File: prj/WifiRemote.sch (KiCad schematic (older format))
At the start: 52 parts, among them J1 DIP-BLACK-MALE-HEADER-VERT_4P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, J2 DIP-BLACK-MALE-HEADER_6P-2.54_, K1 DIP-SWITCH-TACTILE-SPST-NO_TS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, K2 DIP-SWITCH-TACTILE-SPST-NO_TS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, K3 DIP-SWITCH-TACTILE-SPST-NO_TS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, K4 DIP-SWITCH-TACTILE-SPST-NO_TS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, SW1 DIP-TOGGLE-SWITCH-ON-ON_3+2P-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, U1 CONTROLLER-ESP8266, U2 BOOST-MCP1642B-ADJI/MC-MSOP8

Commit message: Updated ADC input for 3V input (2x AA's)
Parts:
- removed R2: SMD-RES-10K-1%-1_10W_0603_, SeeedOPL-Resistor-2016:R0603, symbol SMD-RES-10K-1%-1_10W_0603_
- added R1: SMD-RES-2.7K-1%-1_16W_0402_, symbol SMD-RES-2.7K-1%-1_16W_0402_
- renumbered C2 to C1, C3 to C2, C4 to C3, C5 to C4, C1 to C5, D3 to D1, D4 to D2, D1 to D3, D2 to D4, R12 to R11, R13 to R12, R14 to R13, R16 to R14, R1 to R15, R4 to R16, R11 to R17, R15 to R18, R17 to R19, R3 to R2, R18 to R20, R19 to R21, R20 to R22, R21 to R23, R22 to R24, R23 to R25, R6 to R3, R7 to R4, R24 to R6, R25 to R7

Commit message: Added battery monitoring LED, changed ADC resistor divider, and added ESD + reverse polarity protection on battery
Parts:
- removed R1: SMD-RES-2.7K-1%-1_16W_0402_, symbol SMD-RES-2.7K-1%-1_16W_0402_
- removed R9: SMD-RES-1K-1%-1_10W_0603_, SeeedOPL-Resistor-2016:R0603, symbol SMD-RES-1K-1%-1_10W_0603_
- added D?: SMD-LED-CLEAR-RED_0805_, symbol SMD-LED-CLEAR-RED_0805_
- added D?: SMD-Diode-TVS-3.3VMW-15V-SOD-523, Diodes_SMD:SOD-523, symbol SMD-Diode-TVS-3.3VMW-15V-SOD-523
- added Q?: SMD-MOSFET-N-CH-20V-2.1A-CJ2302_SOT-23_, symbol SMD-MOSFET-N-CH-20V-2.1A-CJ2302_SOT-23_
- added R?: SMD-RES-20K-1%-1_10W_0603_, symbol SMD-RES-20K-1%-1_10W_0603_
- added R?: SMD-RES-51K-5%-1_10W_0603_, symbol SMD-RES-51K-5%-1_10W_0603_
- added R?: SMD-RES-10R-5%-1_10W_0603_, SeeedOPL-Resistor-2016:R0603, symbol SMD-RES-10R-5%-1_10W_0603_
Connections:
- wire segments 100 -> 105
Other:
- note added: "Is BATT- a different GND potential?"
- moved on the sheet: C1, C2, C3, D1, D2, L1, R10, R11, R12, R13, R5, R6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

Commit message: Added button debounce, rev polarity prot, updated ESP-12F, added red LED, updated ADC resistor values
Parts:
- removed D6, D8: SMD-Diode-TVS-3.3VMW-15V-SOD-523, Diodes_SMD:SOD-523, symbol SMD-Diode-TVS-3.3VMW-15V-SOD-523
- removed Q?: SMD-MOSFET-N-CH-20V-2.1A-CJ2302_SOT-23_, symbol SMD-MOSFET-N-CH-20V-2.1A-CJ2302_SOT-23_
- added C6, C7, C8, C9: CERAMIC-100NF-50V-10%-X7R_0603_, symbol CERAMIC-100NF-50V-10%-X7R_0603_
- added D12, D13: SMD-Diode-TVS-3.3VMW-15V-SOD-523, Diodes_SMD:SOD-523, symbol SMD-Diode-TVS-3.3VMW-15V-SOD-523
- added Q1: SMD-MOSFET-P-CH-20V-2A-FDN340P_SOT-23_, symbol SMD-MOSFET-P-CH-20V-2A-FDN340P_SOT-23_
- added R27, R28, R29, R30: SMD-RES-200R-5%-1_10W_0603_, symbol SMD-RES-200R-5%-1_10W_0603_
- R6, R7: RESISTANCE 10 -> 10R
- R8: renamed from R?; RESISTANCE 10 -> 10R
- U1: PART NUMBER ESP-12E -> ESP-12F; SKU 310060021 -> 317060163; SUPPLIER ITEAD -> (none); SUPPLIER PART ESP-12E -> (none)
- gave numbers to parts that had none: 4
- renumbered D12 to D14, D3 to D5, D4 to D6, D5 to D7, D7 to D8, R10 to R11, R11 to R12, R12 to R13, R13 to R14, R14 to R15, R15 to R16, R16 to R17, R17 to R18, R18 to R19, R19 to R20, R20 to R21, R21 to R22, R22 to R23, R23 to R24, R24 to R25, R25 to R26, R8 to R9
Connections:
- wire segments 105 -> 128
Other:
- note removed: "Is BATT- a different GND potential?"
- moved on the sheet: D11, D14, D7, D8, D9, K1, K2, K3, K4, R21, R22, R23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

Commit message: Updated footprints and removed ESP-12F incorrect footprint
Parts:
- C6, C7, C8, C9: footprint (none) -> SeeedOPL-Capacitor-2016:C0603
- D3: footprint (none) -> SeeedOPL-LED-2016:LED-0805
- Q1: footprint (none) -> SeeedOPL-Transistor-2016:SOT-23
- R1, R10, R27, R28, R29, R30: footprint (none) -> SeeedOPL-Resistor-2016:R0603
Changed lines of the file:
@@
 F 0 "R10" V 6550 1650 45  0000 L BNN
 F 1 "SMD-RES-20K-1%-1_10W_0603_" H 6400 1500 45  0001 L BNN
-F 2 "" H 6550 1600 40  0001 C CNN
+F 2 "SeeedOPL-Resistor-2016:R0603" H 6550 1600 40  0001 C CNN
 F 3 "" H 6550 1600 40  0001 C CNN
 F 4 "RC0603FR-0720KL" H 6580 1750 20  0001 C CNN "MPN"
@@
 F 0 "R1" V 6550 1250 45  0000 L BNN
 F 1 "SMD-RES-51K-5%-1_10W_0603_" H 6400 1100 45  0001 L BNN
-F 2 "" H 6550 1200 40  0001 C CNN
+F 2 "SeeedOPL-Resistor-2016:R0603" H 6550 1200 40  0001 C CNN
 F 3 "" H 6550 1200 40  0001 C CNN
 F 4 "RC0603JR-0751KL" H 6580 1350 20  0001 C CNN "MPN"
@@
 F 0 "D3" V 5950 1225 45  0000 L BNN
 F 1 "SMD-LED-CLEAR-RED_0805_" H 5800 1025 45  0001 L BNN
-F 2 "" H 6000 1225 60  0001 C CNN
+F 2 "SeeedOPL-LED-2016:LED-0805" H 6000 1225 60  0001 C CNN
 F 3 "" H 6000 1225 60  0001 C CNN
 F 4 "17-215SURC_S530-A2_TR8" V 6100 1475 20  0000 C CNN "MPN"
@@
 F 0 "Q1" V 825 2050 45  0000 L BNN
 F 1 "SMD-MOSFET-P-CH-20V-2A-FDN340P_SOT-23_" H 950 2250 45  0001 L BNN
-F 2 "" H 950 2150 60  0001 C CNN
+F 2 "SeeedOPL-Transistor-2016:SOT-23" H 950 2150 60  0001 C CNN
 F 3 "" H 950 2150 60  0001 C CNN
 F 4 "FDN340P" H 980 2300 20  0001 C CNN "MPN"
@@
 F 0 "R30" H 4075 4775 45  0000 L BNN
 F 1 "SMD-RES-200R-5%-1_10W_0603_" H 3975 4625 45  0001 L BNN
-F 2 "" H 4125 4725 40  0001 C CNN
+F 2 "SeeedOPL-Resistor-2016:R0603" H 4125 4725 40  0001 C CNN
 F 3 "" H 4125 4725 40  0001 C CNN
 F 4 "RC0603JR-07200RL" H 4155 4875 20  0001 C CNN "MPN"
@@
 F 0 "C9" H 3775 4950 45  0000 L BNN
 F 1 "CERAMIC-100NF-50V-10%-X7R_0603_" H 3575 4825 45  0001 L BNN
-F 2 "" H 3725 4925 60  0001 C CNN
+F 2 "SeeedOPL-Capacitor-2016:C0603" H 3725 4925 60  0001 C CNN
 F 3 "" H 3725 4925 60  0001 C CNN
 F 4 "CC0603KRX7R9BB104" H 3755 5075 20  0001 C CNN "MPN"
@@
 F 0 "C8" H 2950 4725 45  0000 L BNN
 F 1 "CERAMIC-100NF-50V-10%-X7R_0603_" H 2750 4600 45  0001 L BNN
-F 2 "" H 2900 4700 60  0001 C CNN
+F 2 "SeeedOPL-Capacitor-2016:C0603" H 2900 4700 60  0001 C CNN
 F 3 "" H 2900 4700 60  0001 C CNN
 F 4 "CC0603KRX7R9BB104" H 2930 4850 20  0001 C CNN "MPN"
@@
 F 0 "R29" H 3225 4525 45  0000 L BNN
 F 1 "SMD-RES-200R-5%-1_10W_0603_" H 3125 4375 45  0001 L BNN
-F 2 "" H 3275 4475 40  0001 C CNN
+F 2 "SeeedOPL-Resistor-2016:R0603" H 3275 4475 40  0001 C CNN
 F 3 "" H 3275 4475 40  0001 C CNN
 F 4 "RC0603JR-07200RL" H 3305 4625 20  0001 C CNN "MPN"
@@
 F 0 "C7" H 2125 4500 45  0000 L BNN
 F 1 "CERAMIC-100NF-50V-10%-X7R_0603_" H 1925 4375 45  0001 L BNN
-F 2 "" H 2075 4475 60  0001 C CNN
+F 2 "SeeedOPL-Capacitor-2016:C0603" H 2075 4475 60  0001 C CNN
 F 3 "" H 2075 4475 60  0001 C CNN
 F 4 "CC0603KRX7R9BB104" H 2105 4625 20  0001 C CNN "MPN"
@@
 F 0 "R28" H 2400 4275 45  0000 L BNN
 F 1 "SMD-RES-200R-5%-1_10W_0603_" H 2300 4125 45  0001 L BNN
-F 2 "" H 2450 4225 40  0001 C CNN
+F 2 "SeeedOPL-Resistor-2016:R0603" H 2450 4225 40  0001 C CNN
 F 3 "" H 2450 4225 40  0001 C CNN
 F 4 "RC0603JR-07200RL" H 2480 4375 20  0001 C CNN "MPN"
@@
 F 0 "C6" H 1250 4275 45  0000 L BNN
 F 1 "CERAMIC-100NF-50V-10%-X7R_0603_" H 1050 4150 45  0001 L BNN
-F 2 "" H 1200 4250 60  0001 C CNN
+F 2 "SeeedOPL-Capacitor-2016:C0603" H 1200 4250 60  0001 C CNN
 F 3 "" H 1200 4250 60  0001 C CNN
 F 4 "CC0603KRX7R9BB104" H 1230 4400 20  0001 C CNN "MPN"
@@
 F 0 "R27" H 1575 4025 45  0000 L BNN
 F 1 "SMD-RES-200R-5%-1_10W_0603_" H 1475 3875 45  0001 L BNN
-F 2 "" H 1625 3975 40  0001 C CNN
+F 2 "SeeedOPL-Resistor-2016:R0603" H 1625 3975 40  0001 C CNN
 F 3 "" H 1625 3975 40  0001 C CNN
 F 4 "RC0603JR-07200RL" H 1655 4125 20  0001 C CNN "MPN"

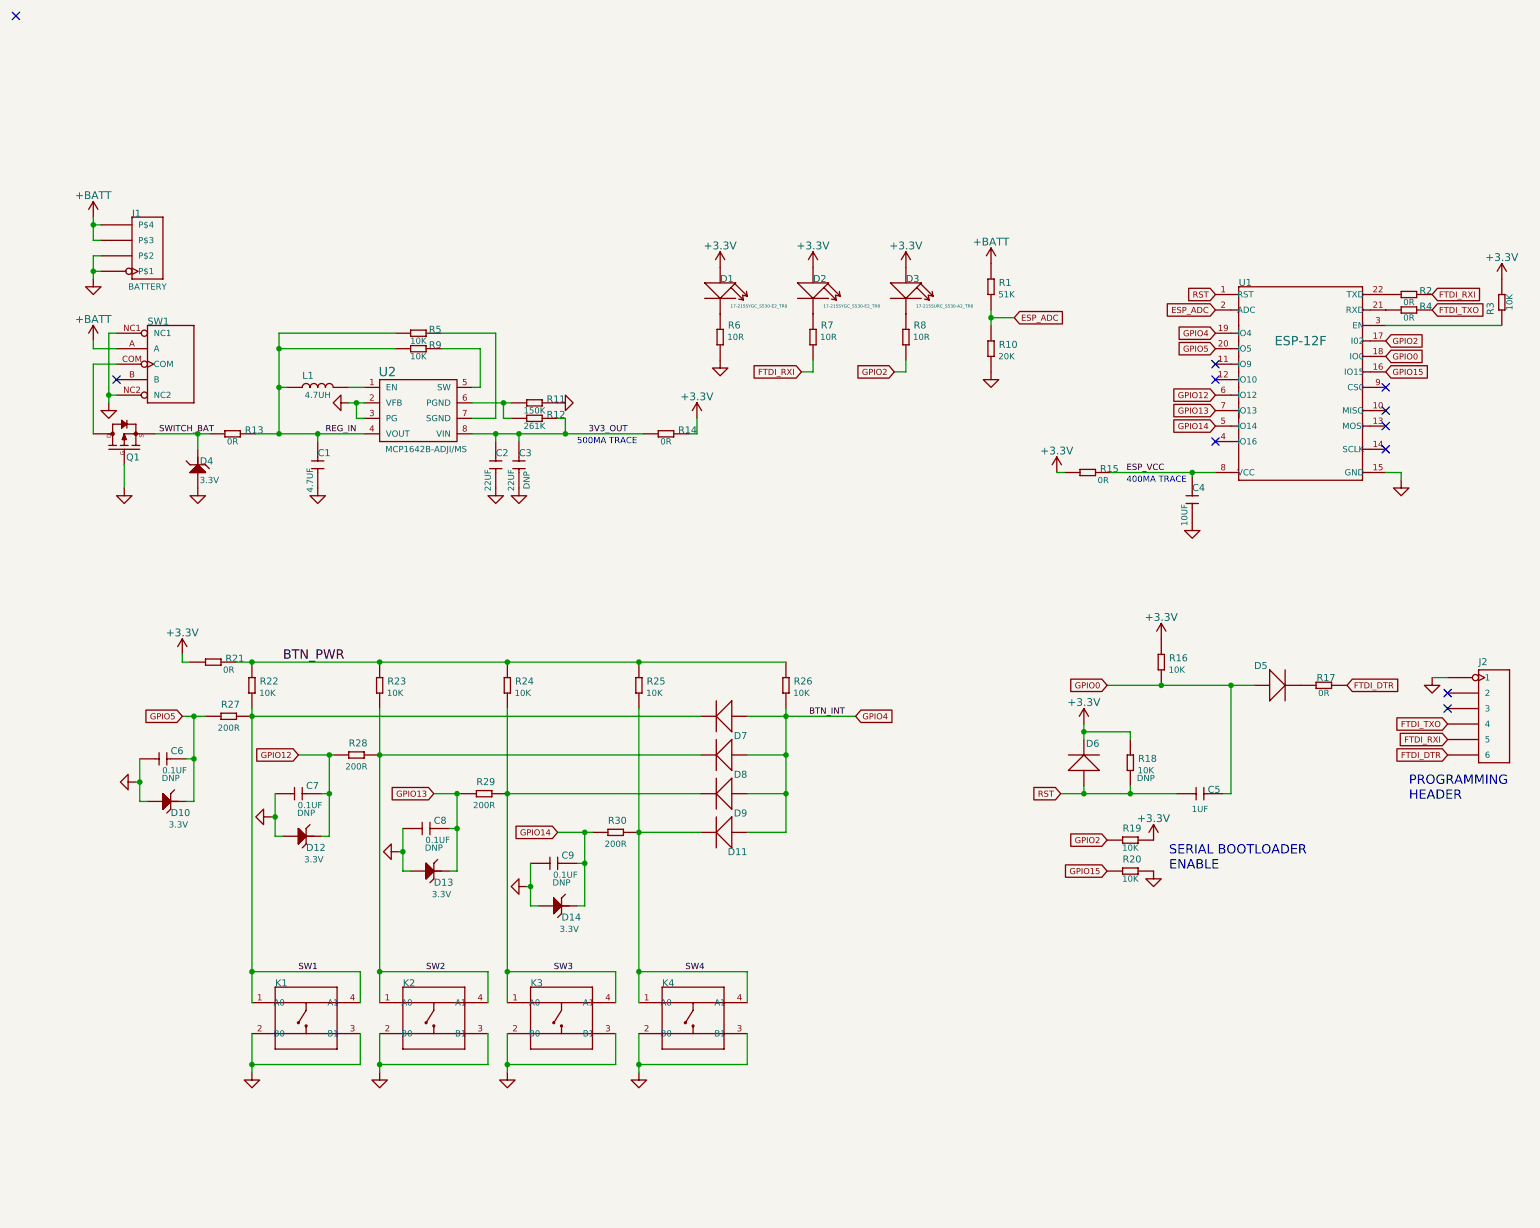
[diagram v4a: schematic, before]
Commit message: Fixed regulator pinout, added mechanical mounts to schematic
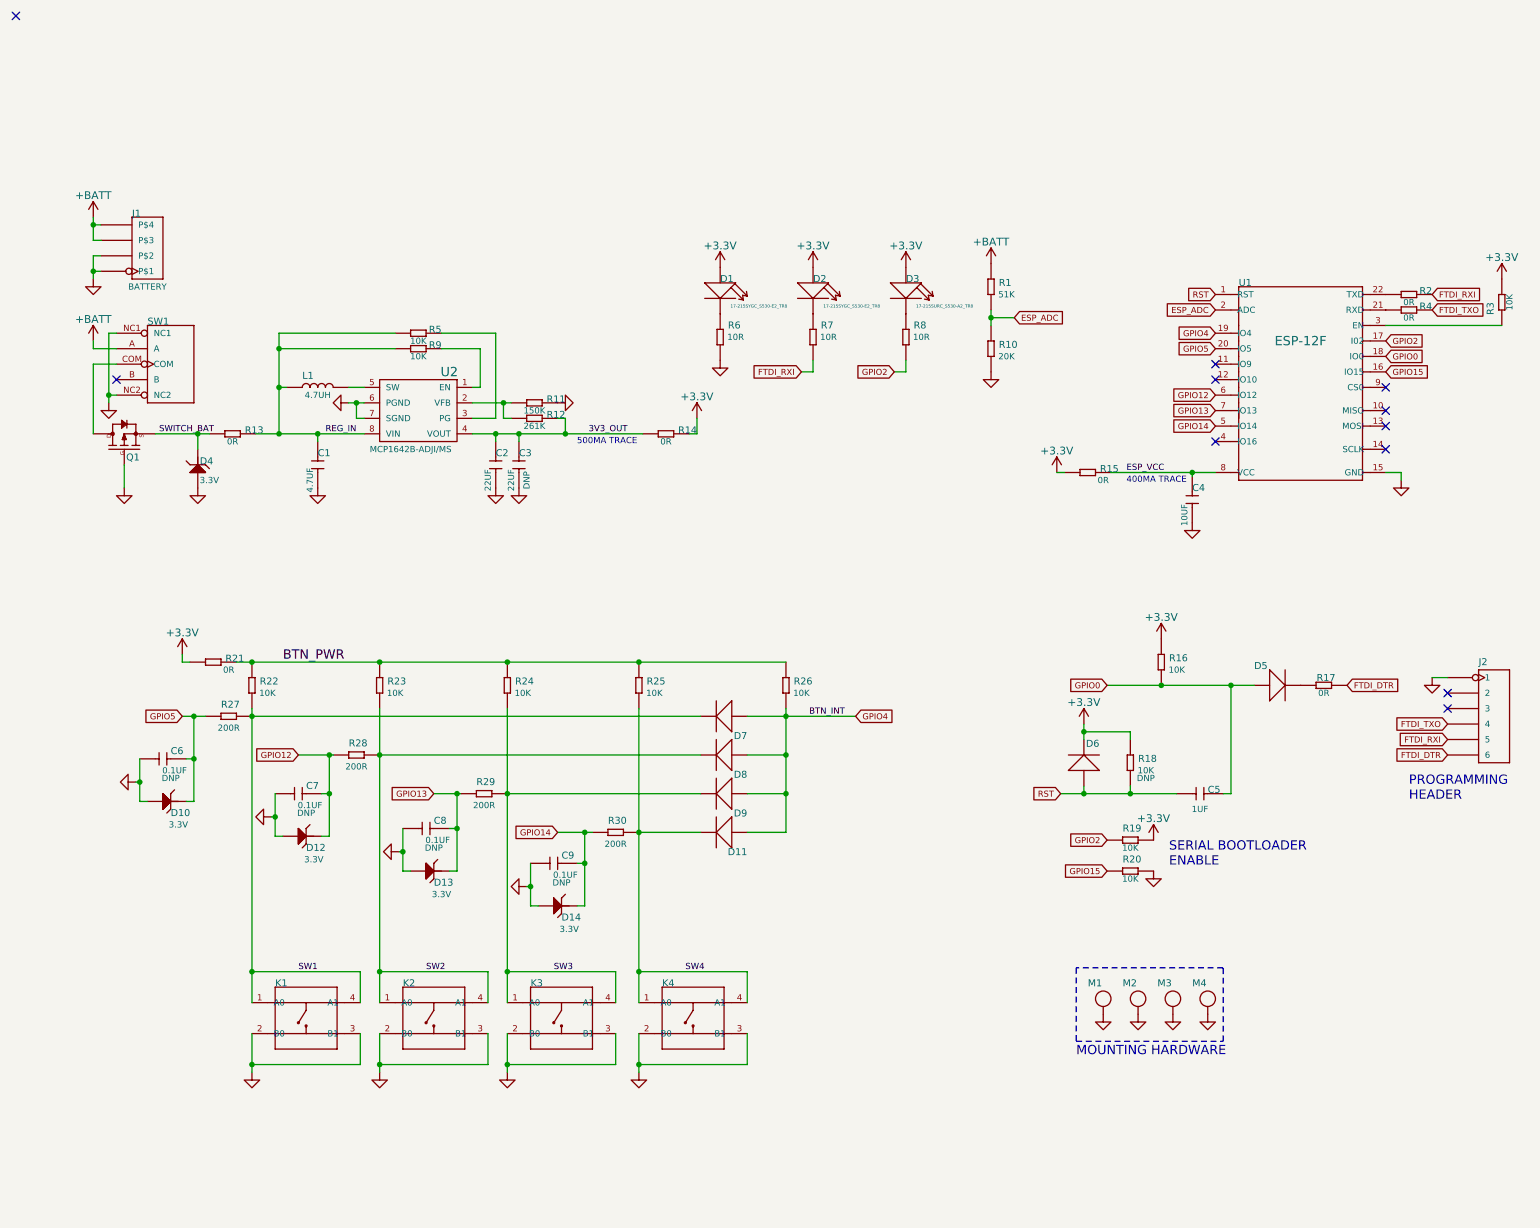
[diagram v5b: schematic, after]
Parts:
- added M1, M2, M3, M4: Mechanical_Mount, symbol Mechanical_Mount
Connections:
- net 3V3_OUT: now also U2.4 (VOUT); no longer U2.8 (VIN)
- net GNDD: now also U2.6 (PGND), U2.7 (SGND), M1.~, M2.~, M3.~, M4.~; no longer U2.2 (VFB), U2.3 (PG)
- net REG_IN: now also U2.8 (VIN); no longer U2.4 (VOUT)
- net at R11.2, R12.2: now also U2.2 (VFB); no longer U2.6 (PGND)
- net at L1.2: now also U2.5 (SW); no longer U2.1 (EN)
- net at R9.1: now also U2.1 (EN); no longer U2.5 (SW)
- net at R5.1: now also U2.3 (PG); no longer U2.7 (SGND)
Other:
- note added: "MOUNTING HARDWARE"
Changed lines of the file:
@@
 LIBS:ICEE-Regulator
 LIBS:ICEE-Diode
+LIBS:ICEE-Mechanical
 EELAYER 25 0
 EELAYER END
@@
 Text Notes 9250 4525 0    60   ~ 0
 PROGRAMMING \nHEADER
-Text Notes 7700 4975 0    60   ~ 0
+Text Notes 7700 4950 0    60   ~ 0
 SERIAL BOOTLOADER \nENABLE
 $Comp
@@
 F 7 "579-MCP1642B-ADJI/MS" H 3050 2650 60  0001 C CNN "SUPPLIER PART"
 	1    2850 2000
-	1    0    0    -1
+	-1   0    0    -1
 $EndComp
 Text Notes 3875 2225 0    40   ~ 0
@@
 	3750 2050 3800 2050
 Wire Wire Line
-	3800 2050 3800 2150
+	3800 2150 3800 2050
 Wire Wire Line
 	3500 2150 3500 2200
@@
 Wire Wire Line
 	4675 3975 1775 3975
+$Comp
+L Mechanical_Mount M1
+U 1 1 59BB9484
+P 7275 5800
+F 0 "M1" H 7175 5875 45  0000 L BNN
+F 1 "Mechanical_Mount" H 7075 5600 45  0001 L BNN
+F 2 "" H 7275 5800 60  0001 C CNN
+F 3 "" H 7275 5800 60  0001 C CNN
+	1    7275 5800
+	1    0    0    -1
+$EndComp
+$Comp
+L Mechanical_Mount M2
+U 1 1 59BB9AA5
+P 7500 5800
+F 0 "M2" H 7400 5875 45  0000 L BNN
+F 1 "Mechanical_Mount" H 7300 5600 45  0001 L BNN
+F 2 "" H 7500 5800 60  0001 C CNN
+F 3 "" H 7500 5800 60  0001 C CNN
+	1    7500 5800
+	1    0    0    -1
+$EndComp
+$Comp
+L Mechanical_Mount M3
+U 1 1 59BB9B95
+P 7725 5800
+F 0 "M3" H 7625 5875 45  0000 L BNN
+F 1 "Mechanical_Mount" H 7525 5600 45  0001 L BNN
+F 2 "" H 7725 5800 60  0001 C CNN
+F 3 "" H 7725 5800 60  0001 C CNN
+	1    7725 5800
+	1    0    0    -1
+$EndComp
+$Comp
+L GNDD #PWR?
+U 1 1 59BC0554
+P 7275 5900
+F 0 "#PWR?" H 7275 5650 50  0001 C CNN
+F 1 "GNDD" H 7275 5750 50  0001 C CNN
+F 2 "" H 7275 5900 50  0000 C CNN
+F 3 "" H 7275 5900 50  0000 C CNN
+	1    7275 5900
+	1    0    0    -1
+$EndComp
+$Comp
+L GNDD #PWR?
+U 1 1 59BC09E3
+P 7500 5900
+F 0 "#PWR?" H 7500 5650 50  0001 C CNN
+F 1 "GNDD" H 7500 5750 50  0001 C CNN
+F 2 "" H 7500 5900 50  0000 C CNN
+F 3 "" H 7500 5900 50  0000 C CNN
+	1    7500 5900
+	1    0    0    -1
+$EndComp
+$Comp
+L GNDD #PWR?
+U 1 1 59BC0C67
+P 7950 5900
+F 0 "#PWR?" H 7950 5650 50  0001 C CNN
+F 1 "GNDD" H 7950 5750 50  0001 C CNN
+F 2 "" H 7950 5900 50  0000 C CNN
+F 3 "" H 7950 5900 50  0000 C CNN
+	1    7950 5900
+	1    0    0    -1
+$EndComp
+$Comp
+L Mechanical_Mount M4
+U 1 1 59BBA5DF
+P 7950 5800
+F 0 "M4" H 7850 5875 45  0000 L BNN
+F 1 "Mechanical_Mount" H 7750 5600 45  0001 L BNN
+F 2 "" H 7950 5800 60  0001 C CNN
+F 3 "" H 7950 5800 60  0001 C CNN
+	1    7950 5800
+	1    0    0    -1
+$EndComp
+$Comp
+L GNDD #PWR?
+U 1 1 59BC0B90
+P 7725 5900
+F 0 "#PWR?" H 7725 5650 50  0001 C CNN
+F 1 "GNDD" H 7725 5750 50  0001 C CNN
+F 2 "" H 7725 5900 50  0000 C CNN
+F 3 "" H 7725 5900 50  0000 C CNN
+	1    7725 5900
+	1    0    0    -1
+$EndComp
+Wire Notes Line
+	7100 5600 7100 6075
+Wire Notes Line
+	7100 6075 8050 6075
+Wire Notes Line
+	8050 6075 8050 5600
+Wire Notes Line
+	8050 5600 7100 5600
+Text Notes 7100 6175 0    60   ~ 0
+MOUNTING HARDWARE
 $EndSCHEMATC
